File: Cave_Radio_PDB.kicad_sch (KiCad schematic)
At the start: 1 part, among them U1 TPS25751D

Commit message: add PD controller first draft
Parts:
- removed U1: TPS25751D, Cave_Radio_PDB:Texas_REF0038A_WQFN-38-2EP_6x4mm_P0.4, symbol Cave_Radio_PDB:TPS25751D
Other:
- added sheet Power (Power.kicad_sch)
- added sheet USB (USB.kicad_sch)
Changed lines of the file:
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@@
 	(generator "eeschema")
 	(generator_version "9.0")
-	(paper "A4")
+	(paper "A3")
 	(title_block
 		(title "Cave Radio PDB")
@@
 		(company "Evan Peters VE7ITX")
 	)
-	(symbol
-		(lib_id "Cave_Radio_PDB:TPS25751D")
-		(at 160.02 95.25 0)
-		(unit 1)
+	(sheet
+		(at 152.4 119.38)
+		(size 43.18 27.94)
 		(exclude_from_sim no)
 		(in_bom yes)
@@
 		(dnp no)
 		(fields_autoplaced yes)
-		(property "Reference" "U1"
-			(at 160.02 62.23 0)
+		(stroke
+			(width 0.1524)
+			(type solid)
+		)
+		(fill
+			(color 0 0 0 0.0000)
+		)
+		(property "Sheetname" "Power"
+			(at 152.4 118.6684 0)
 			(effects
 				(font
 					(size 1.27 1.27)
 				)
+				(justify left bottom)
 			)
 		)
-		(property "Value" "TPS25751D"
-			(at 160.02 64.77 0)
+		(property "Sheetfile" "Power.kicad_sch"
+			(at 152.4 147.9046 0)
 			(effects
 				(font
 					(size 1.27 1.27)
 				)
+				(justify left top)
 			)
 		)
-		(property "Footprint" "Cave_Radio_PDB:Texas_REF0038A_WQFN-38-2EP_6x4mm_P0.4"
-			(at 163.83 148.59 0)
+		(instances
+			(project "Cave_Radio_PDB"
+				(path "/925ec001-c1c1-4fd8-a97e-de5f284bf8c5"
+					(page "2")
+				)
+			)
+		)
+	)
+	(sheet
+		(at 245.11 119.38)
+		(size 43.18 27.94)
+		(exclude_from_sim no)
+		(in_bom yes)
+		(on_board yes)
+		(dnp no)
+		(fields_autoplaced yes)
+		(stroke
+			(width 0.1524)
+			(type solid)
+		)
+		(fill
+			(color 0 0 0 0.0000)
+		)
+		(property "Sheetname" "USB"
+			(at 245.11 118.6684 0)
 			(effects
 				(font
 					(size 1.27 1.27)
 				)
-				(hide yes)
+				(justify left bottom)
 			)
 		)
-		(property "Datasheet" "https://www.ti.com/lit/ds/symlink/tps25751.pdf"
-			(at 160.528 134.366 0)
+		(property "Sheetfile" "USB.kicad_sch"
+			(at 245.11 147.9046 0)
 			(effects
 				(font
 					(size 1.27 1.27)
 				)
-				(hide yes)
+				(justify left top)
 			)
-		)
-		(property "Description" "USB Type-C and USB PD Controller, Programmable, QFN-38"
-			(at 160.274 137.414 0)
-			(effects
-				(font
-					(size 1.27 1.27)
-				)
-				(hide yes)
-			)
-		)
-		(pin "34"
-		)
-		(pin "10"
-		)
-		(pin "17"
-		)
-		(pin "18"
-		)
-		(pin "20"
-		)
-		(pin "38"
-		)
-		(pin "32"
-		)
-		(pin "23"
-		)
-		(pin "1"
-		)
-		(pin "4"
-		)
-		(pin "9"
-		)
-		(pin "8"
-		)
-		(pin "16"
-		)
-		(pin "26"
-		)
-		(pin "36"
-		)
-		(pin "6"
-		)
-		(pin "13"
-		)
-		(pin "27"
-		)
-		(pin "15"
-		)
-		(pin "30"
-		)
-		(pin "3"
-		)
-		(pin "28"
-		)
-		(pin "37"
-		)
-		(pin "40"
-		)
-		(pin "2"
-		)
-		(pin "29"
-		)
-		(pin "11"
-		)
-		(pin "12"
-		)
-		(pin "14"
-		)
-		(pin "19"
-		)
-		(pin "31"
-		)
-		(pin "7"
-		)
-		(pin "39"
-		)
-		(pin "5"
 		)
 		(instances
 			(project "Cave_Radio_PDB"
 				(path "/925ec001-c1c1-4fd8-a97e-de5f284bf8c5"
-					(reference "U1")
-					(unit 1)
+					(page "3")
 				)
 			)

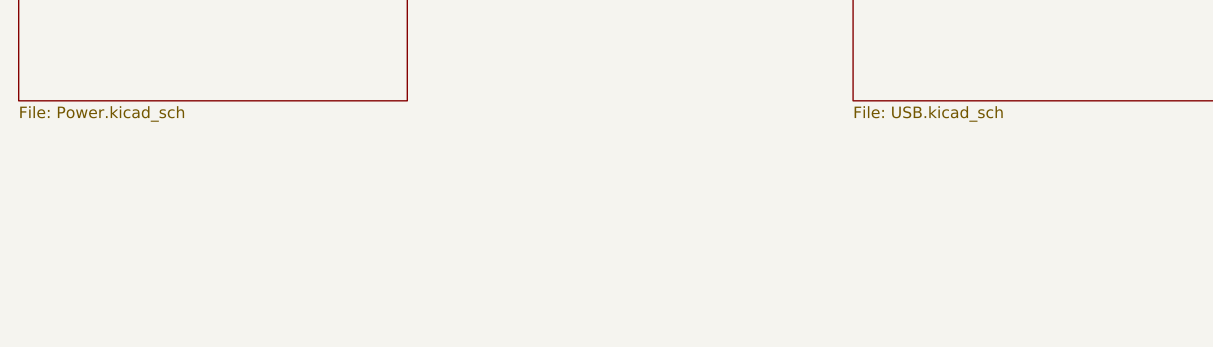
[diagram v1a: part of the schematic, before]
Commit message: start efuse and rough layout
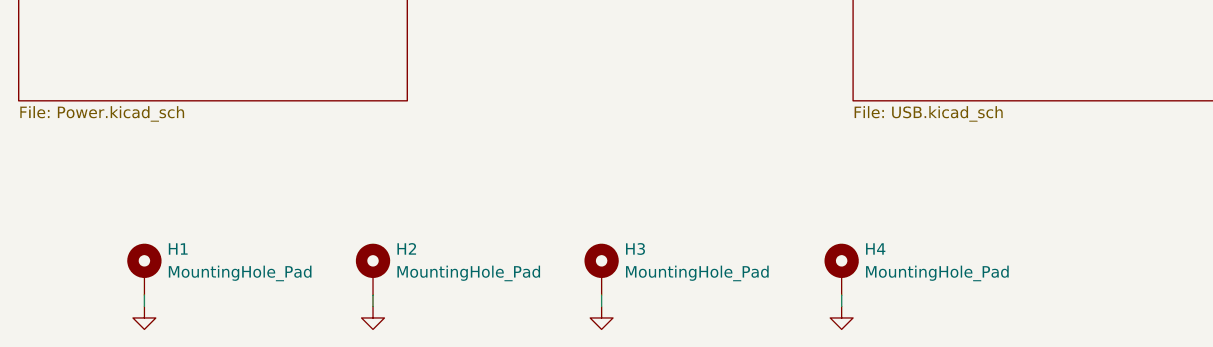
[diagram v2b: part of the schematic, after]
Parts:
- added H1, H2, H3, H4: MountingHole_Pad, Cave_Radio_PDB:MountingHole_3.2mm_M3_DIN965_Pad_TopBottom, symbol Cave_Radio_PDB:MountingHole_Pad
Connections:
- new net GND: H1.1, H2.1, H3.1, H4.1

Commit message: start layout
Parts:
- added H5, H6, H7, H8, H9: Zip_Tie_Support, Cave_Radio_PDB:Zip_Tie_Support, symbol Cave_Radio_PDB:Zip_Tie_Support

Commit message: initial layout
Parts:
- removed H9: Zip_Tie_Support, Cave_Radio_PDB:Zip_Tie_Support, symbol Cave_Radio_PDB:Zip_Tie_Support
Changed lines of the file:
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@@
-	)
-	(symbol
-		(lib_id "Cave_Radio_PDB:Zip_Tie_Support")
-		(at 270.51 186.69 0)
-		(unit 1)
-		(exclude_from_sim no)
-		(in_bom no)
-		(on_board yes)
-		(dnp no)
-		(fields_autoplaced yes)
-		(property "Reference" "H9"
-			(at 273.05 184.1499 0)
-			(effects
-				(font
-					(size 1.27 1.27)
-				)
-				(justify left)
-			)
-		)
-		(property "Value" "Zip_Tie_Support"
-			(at 273.05 186.6899 0)
-			(effects
-				(font
-					(size 1.27 1.27)
-				)
-				(justify left)
-			)
-		)
-		(property "Footprint" "Cave_Radio_PDB:Zip_Tie_Support"
-			(at 270.51 186.69 0)
-			(effects
-				(font
-					(size 1.27 1.27)
-				)
-				(hide yes)
-			)
-		)
-		(property "Datasheet" "~"
-			(at 270.51 186.69 0)
-			(effects
-				(font
-					(size 1.27 1.27)
-				)
-				(hide yes)
-			)
-		)
-		(property "Description" "Zip_Tie_Support"
-			(at 270.51 186.69 0)
-			(effects
-				(font
-					(size 1.27 1.27)
-				)
-				(hide yes)
-			)
-		)
-		(instances
-			(project "Cave_Radio_PDB"
-				(path "/925ec001-c1c1-4fd8-a97e-de5f284bf8c5"
-					(reference "H9")
-					(unit 1)
-				)
-			)
-		)
 	)
 	(symbol
